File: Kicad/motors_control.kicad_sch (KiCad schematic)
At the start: 12 parts, among them M1 Conn_01x02_Pin, M2 Conn_01x02_Pin, U8 TB6612FNG, U9 TB6612FNG

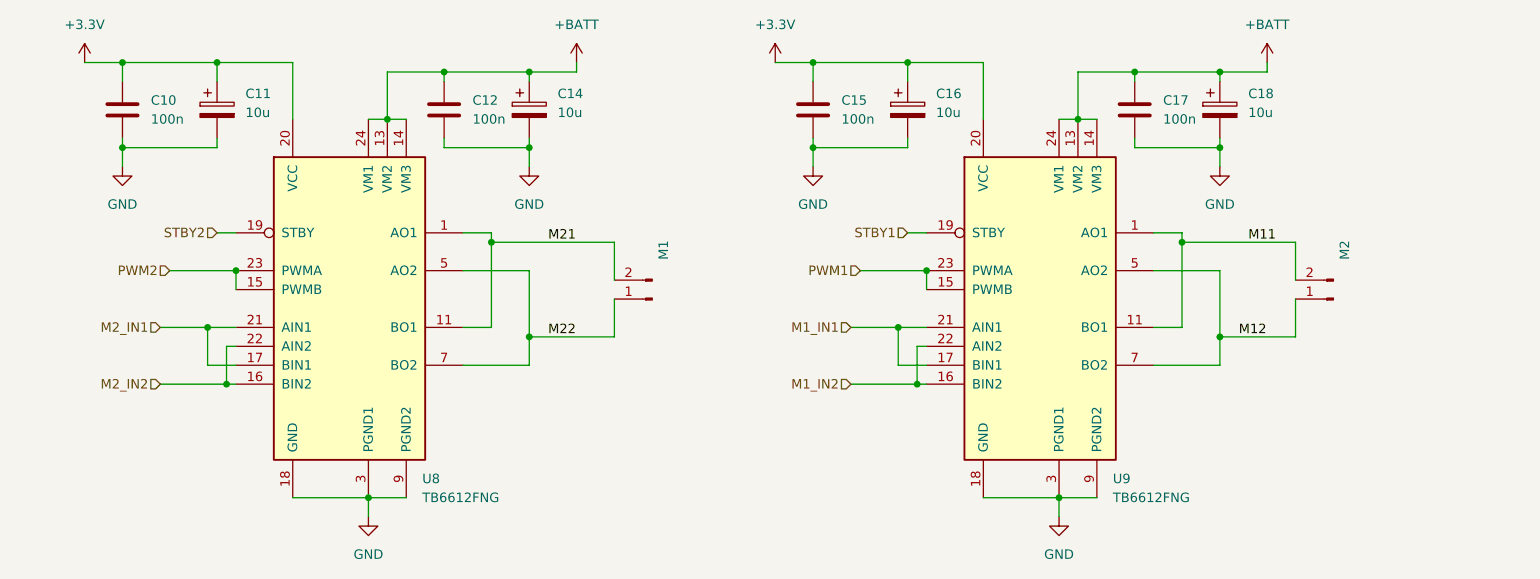
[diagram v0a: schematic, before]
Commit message: finished pcb - added pwm resistors, and fixed VDDA decoupling
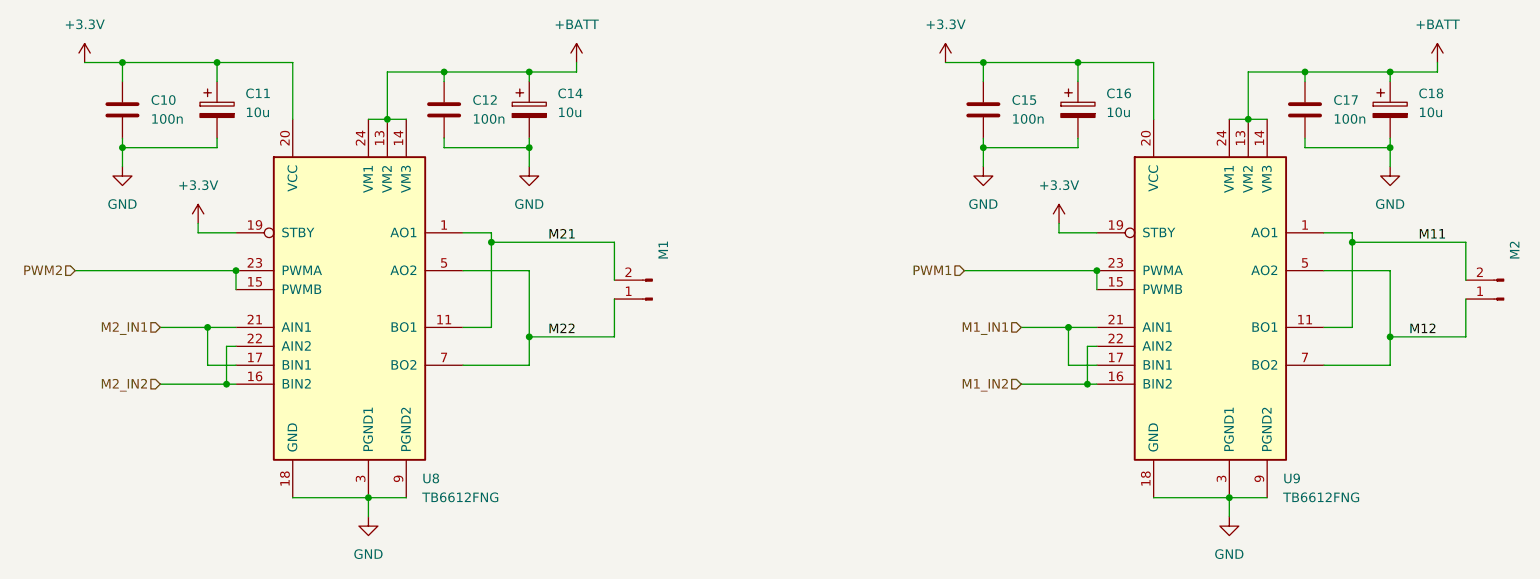
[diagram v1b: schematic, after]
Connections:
- net STBY1 is gone; now on net +3.3V: U9.19 (STBY)
- net STBY2 is gone; now on net +3.3V: U8.19 (STBY)
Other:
- moved on the sheet: C15, C16, C17, C18, M2, U9

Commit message: commit before - fixed start module, in kicad fix -- pcb with new scl1 route and boot0
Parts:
- added R16: 1k5, Resistor_SMD:R_0805_2012Metric_Pad1.20x1.40mm_HandSolder, symbol Device:R
- renumbered M2 to M1, M1 to M2
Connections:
- net GND: now also R16.1
- net PWM1: now also R16.2
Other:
- moved on the sheet: C10, C11

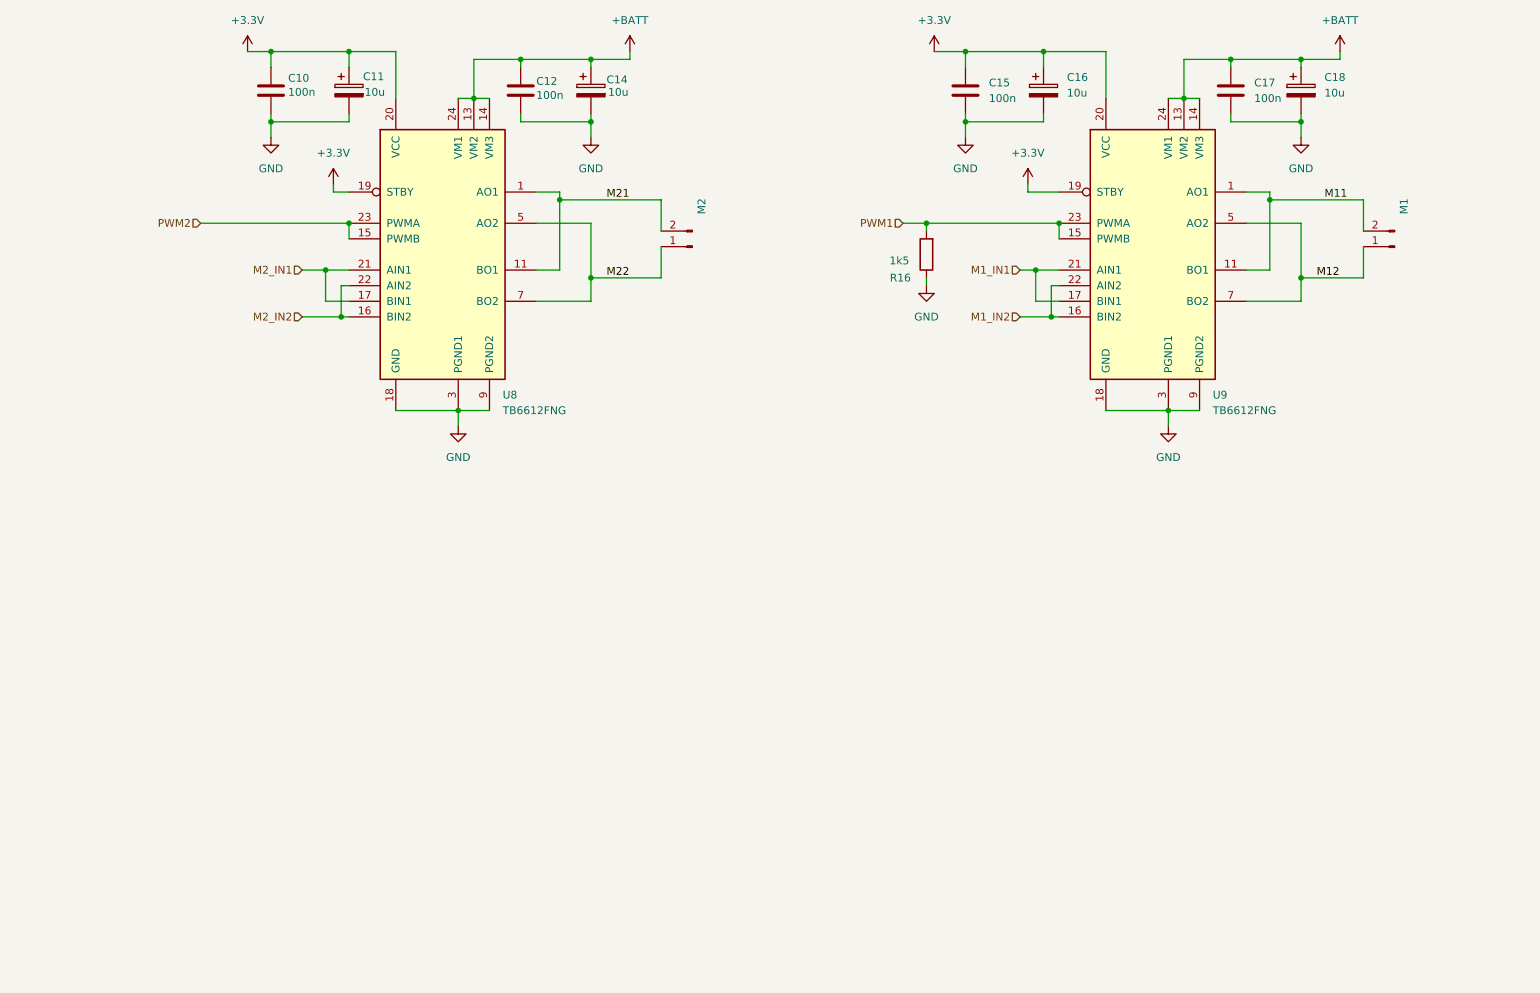
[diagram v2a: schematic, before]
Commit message: kicad schemas documentation
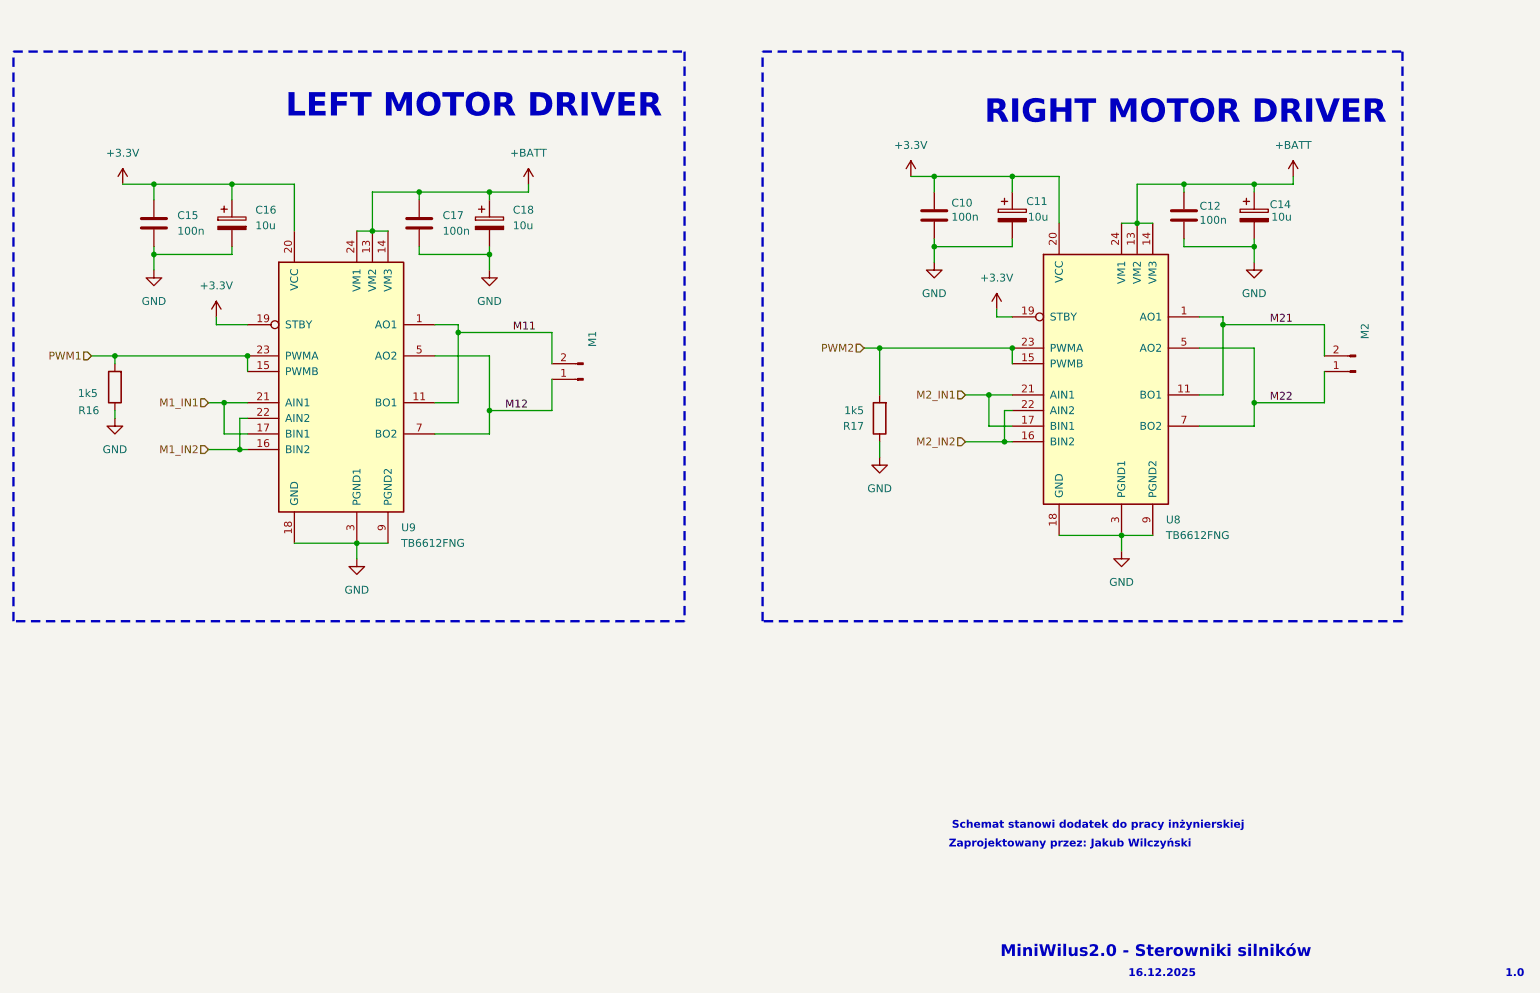
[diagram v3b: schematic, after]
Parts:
- added R17: 1k5, Resistor_SMD:R_0805_2012Metric_Pad1.20x1.40mm_HandSolder, symbol Device:R
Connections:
- net GND: now also R17.1
- net PWM2: now also R17.2
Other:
- note added: "1.0"
- note added: "16.12.2025"
- note added: "LEFT MOTOR DRIVER"
- note added: "MiniWilus2.0 - Sterowniki silników"
- note added: "RIGHT MOTOR DRIVER"
- note added: "Schemat stanowi dodatek do pracy inżynierskiej"
- note added: "Zaprojektowany przez: Jakub Wilczyński"
- moved on the sheet: C10, C11, C12, C14, C15, C16, C17, C18, M1, M2, R16, U8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
